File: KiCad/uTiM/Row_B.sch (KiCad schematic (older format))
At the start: 10 parts, among them U201 APA102, U202 APA102, U203 APA102, U204 APA102, U205 APA102, U206 APA102, U207 APA102, U208 APA102

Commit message: microTiM aka uTiM work in progress
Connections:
- net CO_B renamed CI_C
- net DO_B renamed DI_C
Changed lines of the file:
@@
 DI_B
 Text HLabel 950  3100 0    60   Output ~ 12
-CO_B
+CI_C
 Text HLabel 950  2350 0    60   Input ~ 12
 GND
@@
 5V
 Text Label 1075 3100 0    60   ~ 0
-CO_B
+CI_C
 $Comp
 L C2 C201
@@
 	10950 3350 950  3350
 Text HLabel 950  3350 0    60   Output ~ 12
-DO_B
+DI_C
 Text HLabel 950  1400 0    60   Input ~ 12
 DI_B
@@
 	1300 1600 950  1600
 Text Label 1075 3350 0    60   ~ 0
-DO_B
+DI_C
 Text Label 1075 1600 0    60   ~ 0
 CI_B

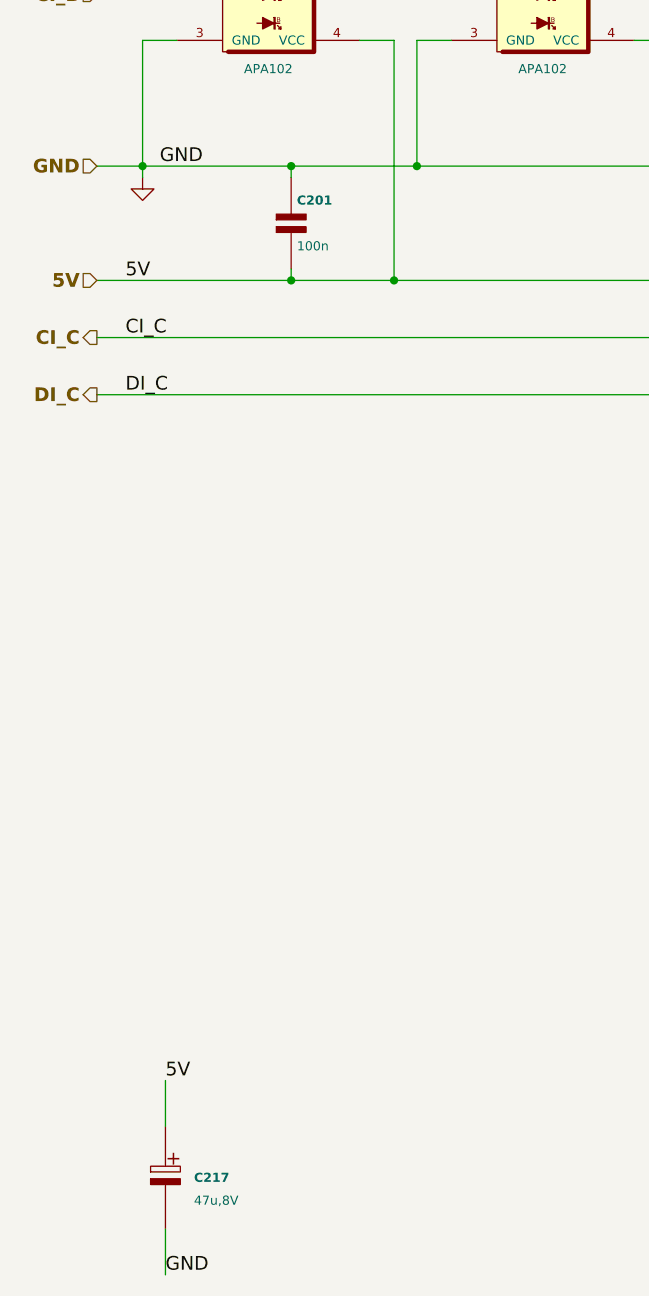
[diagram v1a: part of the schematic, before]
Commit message: work in progress, microTIM using APA102
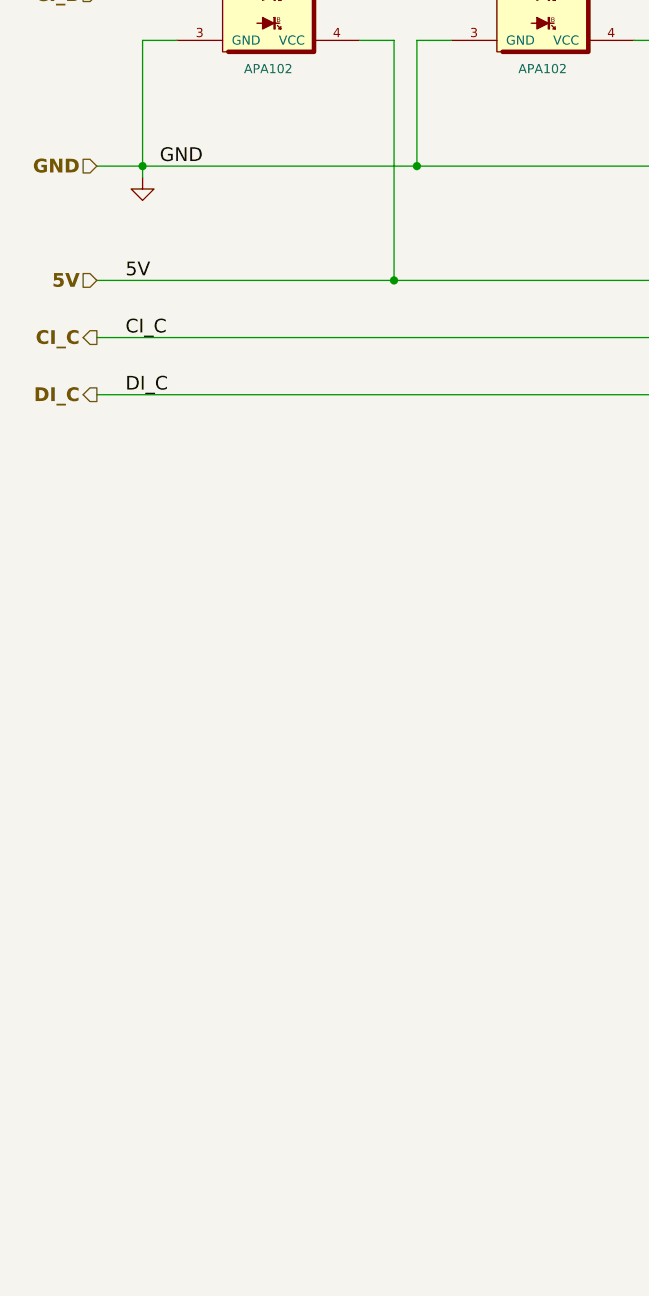
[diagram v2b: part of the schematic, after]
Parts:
- removed C201: 100n, TinyTiM_Libs:c_0805, symbol C2
- removed C217: 47u,8V, TinyTiM_Libs:c_2917, symbol C_POL_1
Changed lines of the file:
@@
 Comment4 ""
 $EndDescr
-Text Label 1250 6350 0    60   ~ 0
-5V
-Text Label 1250 7200 0    60   ~ 0
-GND
-$Comp
-L C_POL_1 C217
-U 1 1 5118AB5B
-P 1250 6750
-F 0 "C217" H 1375 6725 40  0000 L CNB
-F 1 "47u,8V" H 1375 6625 40  0000 L CNN
-F 2 "TinyTiM_Libs:c_2917" H 1250 6700 50  0001 C CNN
-F 3 "" H 1250 6750 60  0001 C CNN
-F 4 "CAP ALUM 47UF 8V 20% SMD" H 1250 6950 60  0001 L CNN "Field4"
-F 5 "47u,8V" H 1250 7050 60  0001 L CNN "Field5"
-F 6 "2917 (7343 Metric)" H 1250 7150 60  0001 L CNN "Field6"
-F 7 "Panasonic Electronic Components" H 1250 7250 60  0001 L CNN "Field7"
-F 8 "EEF-CD0K470R" H 1250 7350 60  0001 L CNN "Field8"
-F 9 "Digikey" H 1250 7450 60  0001 L CNN "Field9"
-F 10 "PCE3606CT-ND" H 1250 7550 60  0001 L CNN "Field10"
-F 11 "http://www.digikey.com/product-detail/en/EEF-CD0K470R/PCE3606CT-ND/614442" H 1250 7650 60  0001 L CNN "Field11"
-	1    1250 6750
-	1    0    0    -1
-$EndComp
-Wire Wire Line
-	1250 7000 1250 7200
-Wire Wire Line
-	1250 6550 1250 6350
 Text Label 1075 1400 0    60   ~ 0
 DI_B
@@
 CI_C
 $Comp
-L C2 C201
-U 1 1 56C2B796
-P 1800 2600
-F 0 "C201" H 1825 2700 40  0000 L CNB
-F 1 "100n" H 1825 2500 40  0000 L CNN
-F 2 "TinyTiM_Libs:c_0805" H 1800 2600 50  0001 C CNN
-F 3 "" H 1800 2600 60  0001 C CNN
-F 4 "CAP CER 0.1UF 25V 10% X7R 0805" H 1800 2800 60  0001 L CNN "Field4"
-F 5 "100nF, 25V" H 1800 2900 60  0001 L CNN "Field5"
-F 6 "Surface Mount, MLCC" H 1800 3000 60  0001 L CNN "Field6"
-F 7 "Kemet" H 1800 3100 60  0001 L CNN "Field7"
-F 8 "C0805C104K3RACTU" H 1800 3200 60  0001 L CNN "Field8"
-F 9 "Digikey" H 1800 3300 60  0001 L CNN "Field9"
-F 10 "399-1168-1-ND" H 1800 3400 60  0001 L CNN "Field10"
-F 11 "http://www.digikey.com/product-detail/en/C0805C104K3RACTU/399-1168-1-ND/411443" H 1800 3500 60  0001 L CNN "Field11"
-	1    1800 2600
-	1    0    0    -1
-$EndComp
-$Comp
 L GND #PWR010
 U 1 1 56C2B79D
@@
 Wire Wire Line
 	1150 1800 1150 2400
-Connection ~ 1800 2850
-Wire Wire Line
-	1800 2850 1800 2800
 Wire Wire Line
 	950  3100 10800 3100
-Connection ~ 1800 2350
 Wire Wire Line
 	950  2350 9550 2350
@@
 	10800 3100 10800 1600
 Wire Wire Line
-	1800 2350 1800 2400
-Wire Wire Line
 	950  2850 10650 2850

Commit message: layout complete. Gerbers pending
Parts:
- renumbered U201 to U09, U202 to U10, U203 to U11, U204 to U12, U205 to U13, U206 to U14, U207 to U15, U208 to U16
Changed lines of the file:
@@
 GND
 $Comp
-L APA102 U201
+L APA102 U09
 U 1 1 56C2B784
 P 1700 1600
-F 0 "U201" H 1700 1900 40  0000 C CNB
+F 0 "U09" H 1700 1900 40  0000 C CNB
 F 1 "APA102" H 1700 1275 40  0000 C CNN
 F 2 "TinyTiM_Libs:APA102" H 1600 2000 60  0001 C CNN
@@
 5V
 $Comp
-L APA102 U202
+L APA102 U10
 U 1 1 56C2B7AF
 P 2900 1600
-F 0 "U202" H 2900 1900 40  0000 C CNB
+F 0 "U10" H 2900 1900 40  0000 C CNB
 F 1 "APA102" H 2900 1275 40  0000 C CNN
 F 2 "TinyTiM_Libs:APA102" H 2800 2000 60  0001 C CNN
@@
 $EndComp
 $Comp
-L APA102 U203
+L APA102 U11
 U 1 1 56C2B7B7
 P 4100 1600
-F 0 "U203" H 4100 1900 40  0000 C CNB
+F 0 "U11" H 4100 1900 40  0000 C CNB
 F 1 "APA102" H 4100 1275 40  0000 C CNN
 F 2 "TinyTiM_Libs:APA102" H 4000 2000 60  0001 C CNN
@@
 $EndComp
 $Comp
-L APA102 U204
+L APA102 U12
 U 1 1 56C2B7BF
 P 5300 1600
-F 0 "U204" H 5300 1900 40  0000 C CNB
+F 0 "U12" H 5300 1900 40  0000 C CNB
 F 1 "APA102" H 5300 1275 40  0000 C CNN
 F 2 "TinyTiM_Libs:APA102" H 5200 2000 60  0001 C CNN
@@
 $EndComp
 $Comp
-L APA102 U205
+L APA102 U13
 U 1 1 56C2B7C7
 P 6500 1600
-F 0 "U205" H 6500 1900 40  0000 C CNB
+F 0 "U13" H 6500 1900 40  0000 C CNB
 F 1 "APA102" H 6500 1275 40  0000 C CNN
 F 2 "TinyTiM_Libs:APA102" H 6400 2000 60  0001 C CNN
@@
 $EndComp
 $Comp
-L APA102 U206
+L APA102 U14
 U 1 1 56C2B7CF
 P 7700 1600
-F 0 "U206" H 7700 1900 40  0000 C CNB
+F 0 "U14" H 7700 1900 40  0000 C CNB
 F 1 "APA102" H 7700 1275 40  0000 C CNN
 F 2 "TinyTiM_Libs:APA102" H 7600 2000 60  0001 C CNN
@@
 $EndComp
 $Comp
-L APA102 U207
+L APA102 U15
 U 1 1 56C2B7D7
 P 8900 1600
-F 0 "U207" H 8900 1900 40  0000 C CNB
+F 0 "U15" H 8900 1900 40  0000 C CNB
 F 1 "APA102" H 8900 1275 40  0000 C CNN
 F 2 "TinyTiM_Libs:APA102" H 8800 2000 60  0001 C CNN
@@
 $EndComp
 $Comp
-L APA102 U208
+L APA102 U16
 U 1 1 56C2B7DF
 P 10100 1600
-F 0 "U208" H 10100 1900 40  0000 C CNB
+F 0 "U16" H 10100 1900 40  0000 C CNB
 F 1 "APA102" H 10100 1275 40  0000 C CNN
 F 2 "TinyTiM_Libs:APA102" H 10000 2000 60  0001 C CNN
